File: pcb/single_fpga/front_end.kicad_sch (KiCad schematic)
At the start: 19 parts, among them J1 Main Power Input, J2 AXK5S80337YG, U1 TLV62569DBV

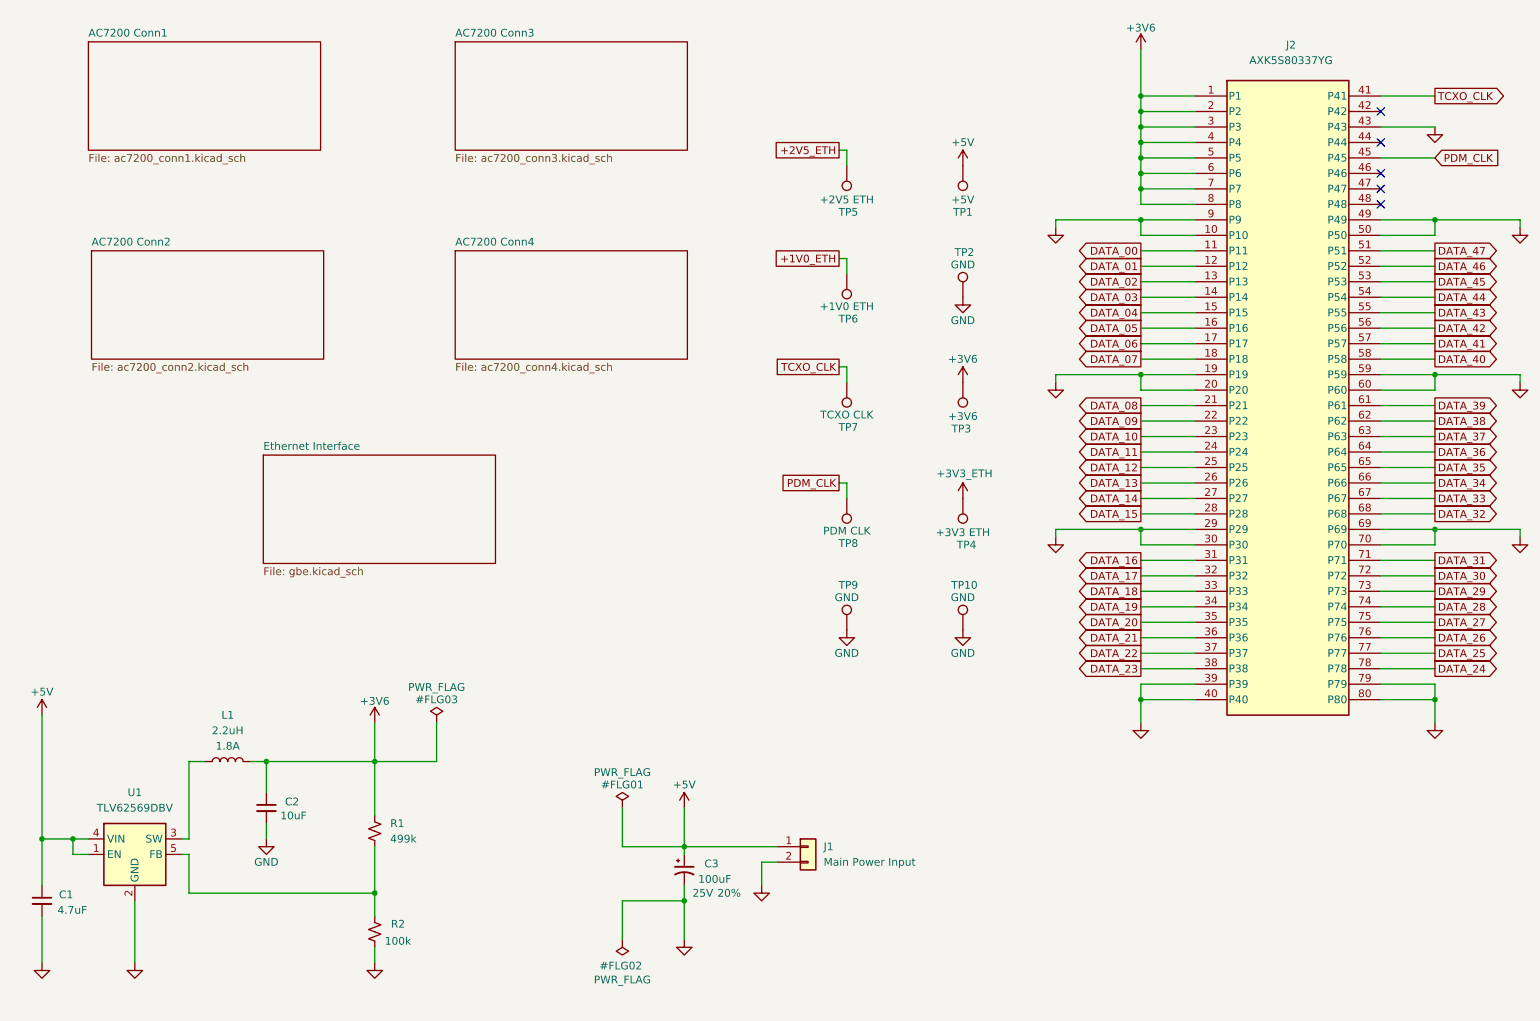
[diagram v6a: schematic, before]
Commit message: Added RGB status LED.
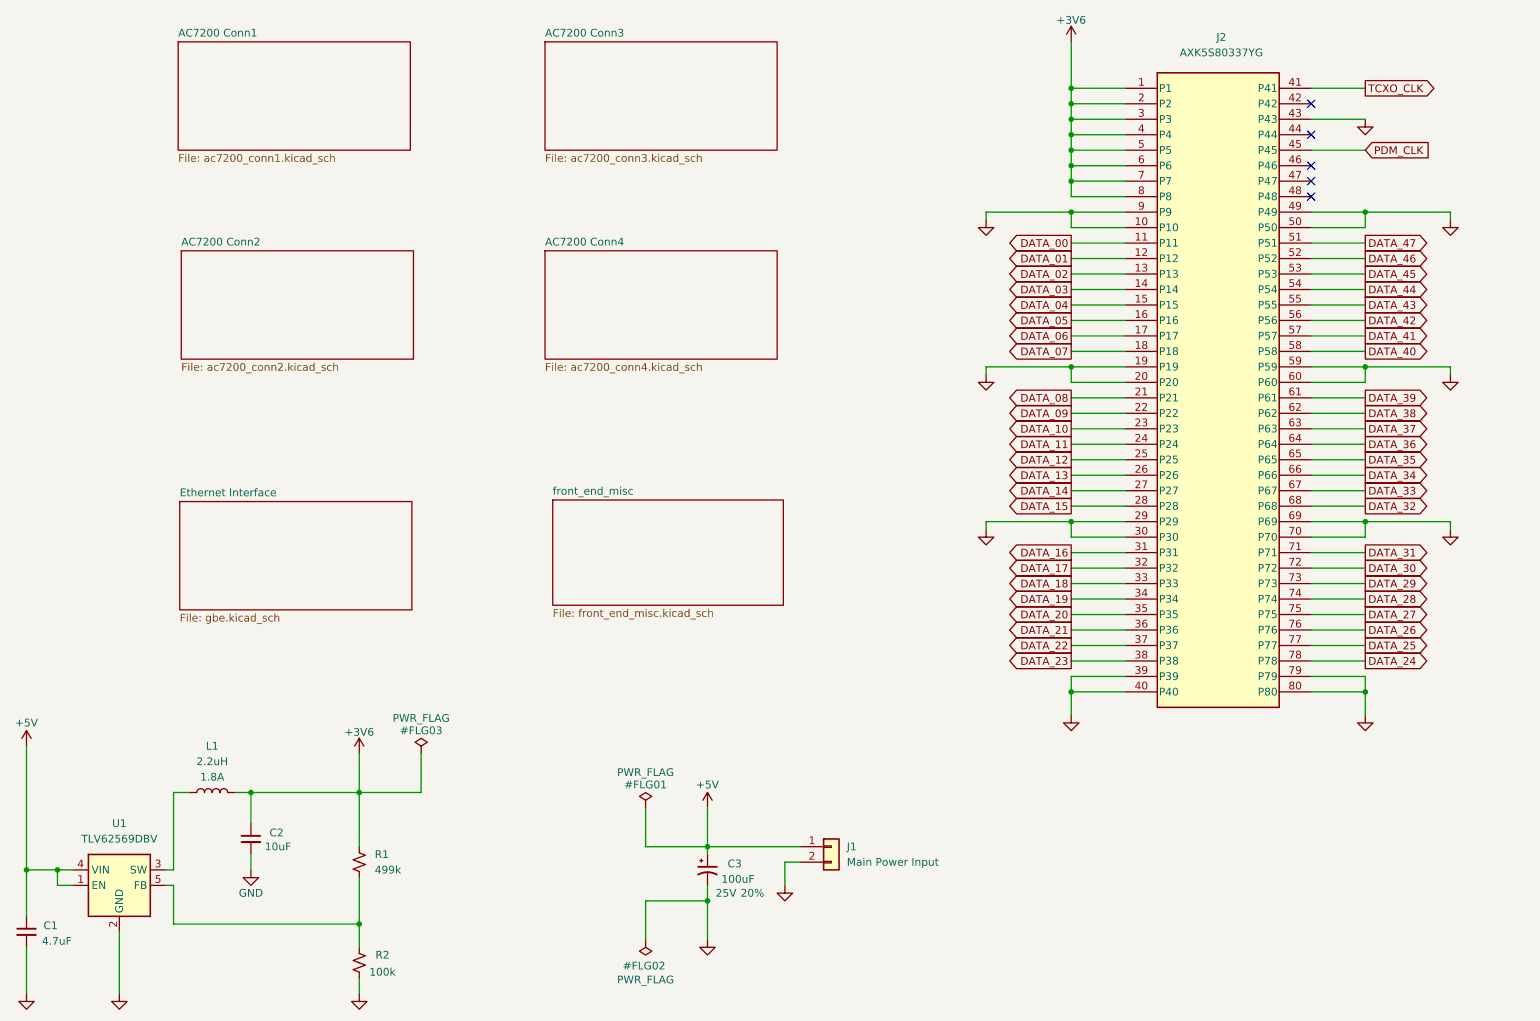
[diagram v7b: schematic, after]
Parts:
- removed TP1: +5V, TestPoint:TestPoint_THTPad_D2.0mm_Drill1.0mm, symbol Connector:TestPoint
- removed TP10, TP2, TP9: GND, TestPoint:TestPoint_THTPad_D2.0mm_Drill1.0mm, symbol Connector:TestPoint
- removed TP3: +3V6, TestPoint:TestPoint_THTPad_D2.0mm_Drill1.0mm, symbol Connector:TestPoint
- removed TP4: +3V3 ETH, TestPoint:TestPoint_THTPad_D2.0mm_Drill1.0mm, symbol Connector:TestPoint
- removed TP5: +2V5 ETH, TestPoint:TestPoint_THTPad_D2.0mm_Drill1.0mm, symbol Connector:TestPoint
- removed TP6: +1V0 ETH, TestPoint:TestPoint_THTPad_D2.0mm_Drill1.0mm, symbol Connector:TestPoint
- removed TP7: TCXO CLK, TestPoint:TestPoint_THTPad_D2.0mm_Drill1.0mm, symbol Connector:TestPoint
- removed TP8: PDM CLK, TestPoint:TestPoint_THTPad_D2.0mm_Drill1.0mm, symbol Connector:TestPoint
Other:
- added sheet front_end_misc (front_end_misc.kicad_sch)
- moved on the sheet: C1, C2, C3, J1, J2, L1, R1, R2, U1
